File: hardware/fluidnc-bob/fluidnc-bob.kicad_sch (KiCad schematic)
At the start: 45 parts, among them J1 5V-IN, J10 LIM-Z, J11 PROBE, J2 X-DRV, J3 Y-DRV, J4 Z-DRV, J5 LIM-X, J6 LIM-Y, J7 RELAY, J8 AUX, J9 SD, Q1 2N7000, U1 SN74HC541N

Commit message: F1: generic 1-2A fast fuse on wire pads instead of polyfuse
Drew is soldering in a glass fuse (multimeter spare) by its pigtails;
the GS1A crowbar still blows it on reverse polarity. ERC clean,
netlist re-verified.

Co-Authored-By: Claude Fable 5 <noreply@anthropic.com>
Claude-Session: https://claude.ai/code/session_01VS3q9dMLBayBFkECVEvZ78
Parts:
- F1: value MF-R110 1.1A -> Fuse 1.5A fast; footprint Fuse:Fuse_Bourns_MF-RG300 -> fluidnc-bob:WirePads_1x02_P5.08mm
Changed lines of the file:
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@@
   (symbol (lib_id "bob:Fuse_H") (at 53.34 96.52 0) (unit 1) (exclude_from_sim no) (in_bom yes) (on_board yes) (dnp no)
     (property "Reference" "F1" (at 55.88 90.17 0) (effects (font (size 1.27 1.27))))
-    (property "Value" "MF-R110 1.1A" (at 55.88 102.86999999999999 0) (effects (font (size 1.27 1.27))))
-    (property "Footprint" "Fuse:Fuse_Bourns_MF-RG300" (at 53.34 96.52 0) (effects (font (size 1.27 1.27)) hide))
+    (property "Value" "Fuse 1.5A fast" (at 55.88 102.86999999999999 0) (effects (font (size 1.27 1.27))))
+    (property "Footprint" "fluidnc-bob:WirePads_1x02_P5.08mm" (at 53.34 96.52 0) (effects (font (size 1.27 1.27)) hide))
     (property "Datasheet" "" (at 53.34 96.52 0) (effects (font (size 1.27 1.27)) hide))
     (pin "1")

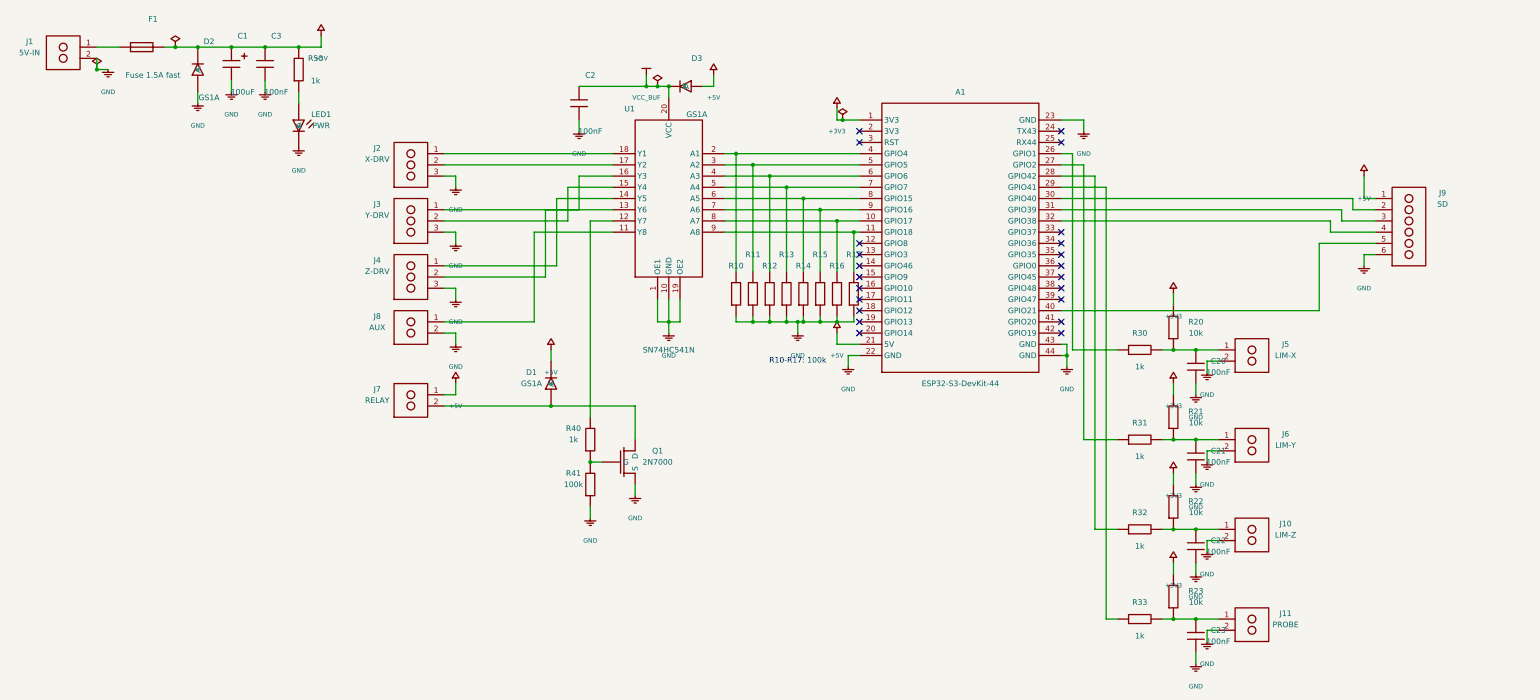
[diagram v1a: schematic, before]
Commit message: Schematic: official KiCad power symbols, labels tight to symbols
GND/+5V/+3V3/PWR_FLAG now come verbatim from KiCad's power library
(only the project-specific VCC_BUF rail stays custom). Ref/value text
placed snug beside each symbol with proper justification instead of
floating above/below. ERC clean, netlist re-verified.

Co-Authored-By: Claude Fable 5 <noreply@anthropic.com>
Claude-Session: https://claude.ai/code/session_01VS3q9dMLBayBFkECVEvZ78
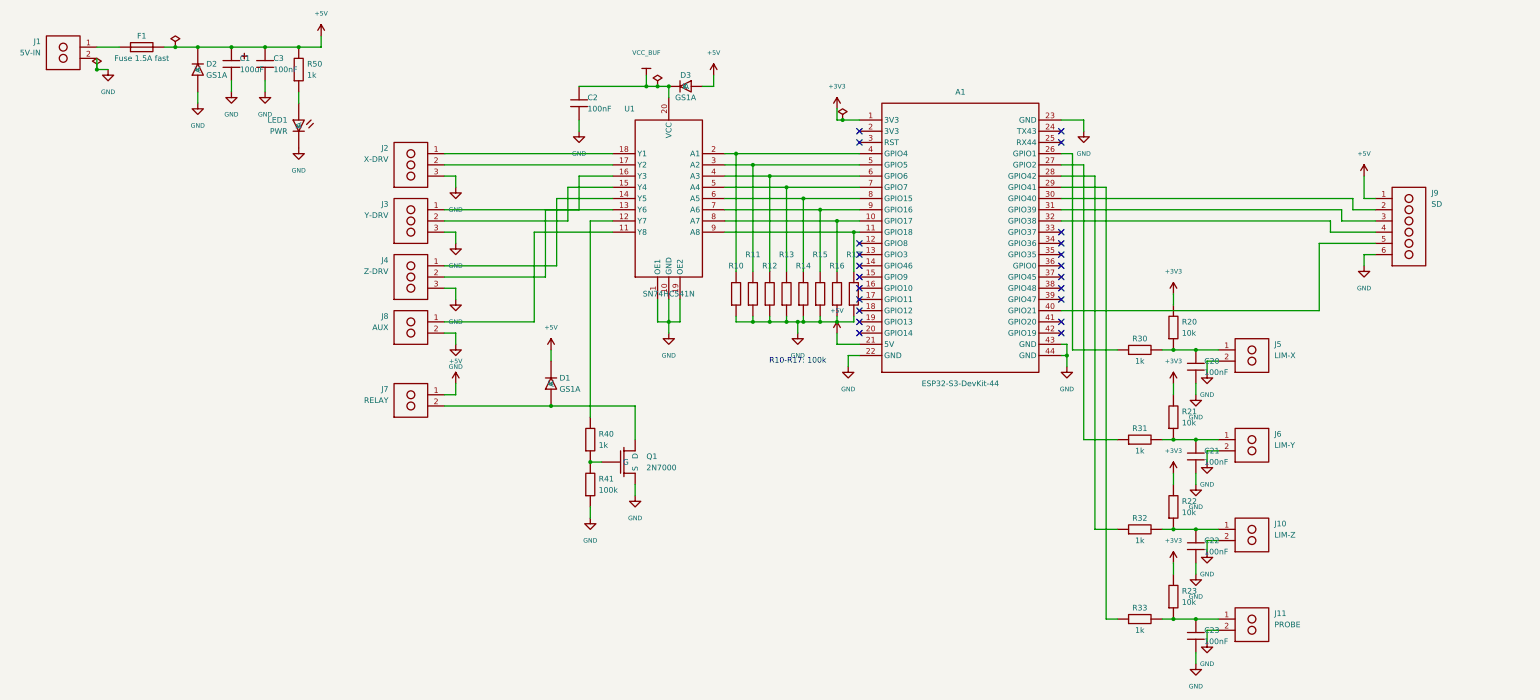
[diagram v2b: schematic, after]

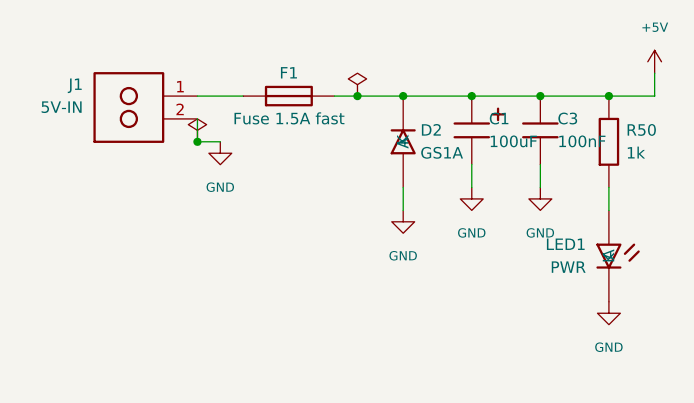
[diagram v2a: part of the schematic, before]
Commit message: F1: Littelfuse 1210L150/16WR PTC polyfuse (found in bin)
1.5A hold / ~3A trip, 16V, 1210 SMD — self-resetting, back to the
original polyfuse intent. ERC clean, netlist re-verified.

Co-Authored-By: Claude Fable 5 <noreply@anthropic.com>
Claude-Session: https://claude.ai/code/session_01VS3q9dMLBayBFkECVEvZ78
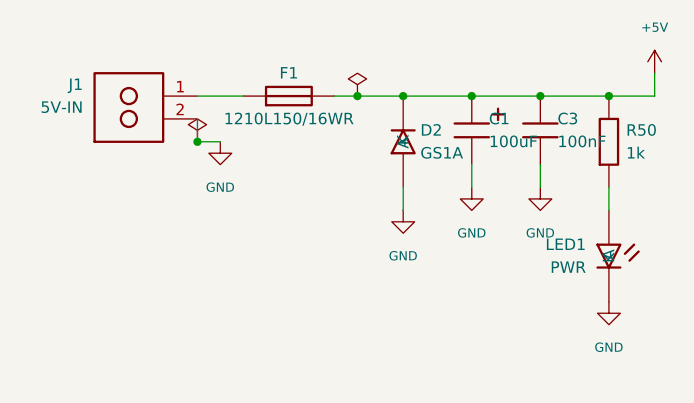
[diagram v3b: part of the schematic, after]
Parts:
- F1: value Fuse 1.5A fast -> 1210L150/16WR; footprint fluidnc-bob:WirePads_1x02_P5.08mm -> Fuse:Fuse_1210_3225Metric
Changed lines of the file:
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@@
   (symbol (lib_id "bob:Fuse_H") (at 53.34 96.52 0) (unit 1) (exclude_from_sim no) (in_bom yes) (on_board yes) (dnp no)
     (property "Reference" "F1" (at 53.34 93.97999999999999 0) (effects (font (size 1.27 1.27))))
-    (property "Value" "Fuse 1.5A fast" (at 53.34 99.06 0) (effects (font (size 1.27 1.27))))
-    (property "Footprint" "fluidnc-bob:WirePads_1x02_P5.08mm" (at 53.34 96.52 0) (effects (font (size 1.27 1.27)) hide))
+    (property "Value" "1210L150/16WR" (at 53.34 99.06 0) (effects (font (size 1.27 1.27))))
+    (property "Footprint" "Fuse:Fuse_1210_3225Metric" (at 53.34 96.52 0) (effects (font (size 1.27 1.27)) hide))
     (property "Datasheet" "" (at 53.34 96.52 0) (effects (font (size 1.27 1.27)) hide))
     (pin "1")

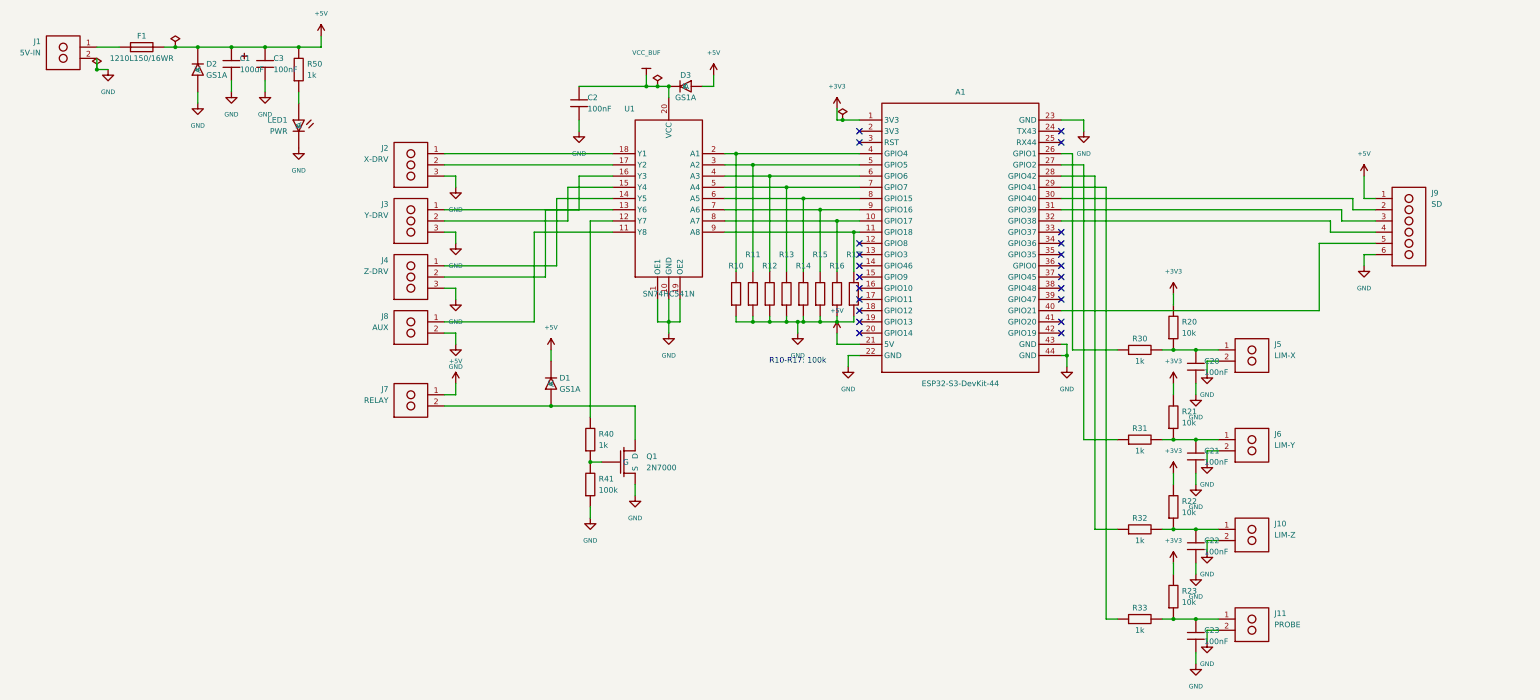
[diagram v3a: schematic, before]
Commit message: Schematic readability: crossing-free right side, labeled outputs
- J9 (SD) moved beside the devkit, straight drops from the SD pins;
  pad order now SCK/MISO/MOSI/CS/5V/GND
- Limit/probe conditioning fanned far right with non-crossing lanes
- U1 outputs use net labels on both ends (XSTEP..AUX1, SPIN5) instead
  of crossing L-wires between buffer and pad groups

ERC clean, netlist re-verified.

Co-Authored-By: Claude Fable 5 <noreply@anthropic.com>
Claude-Session: https://claude.ai/code/session_01VS3q9dMLBayBFkECVEvZ78
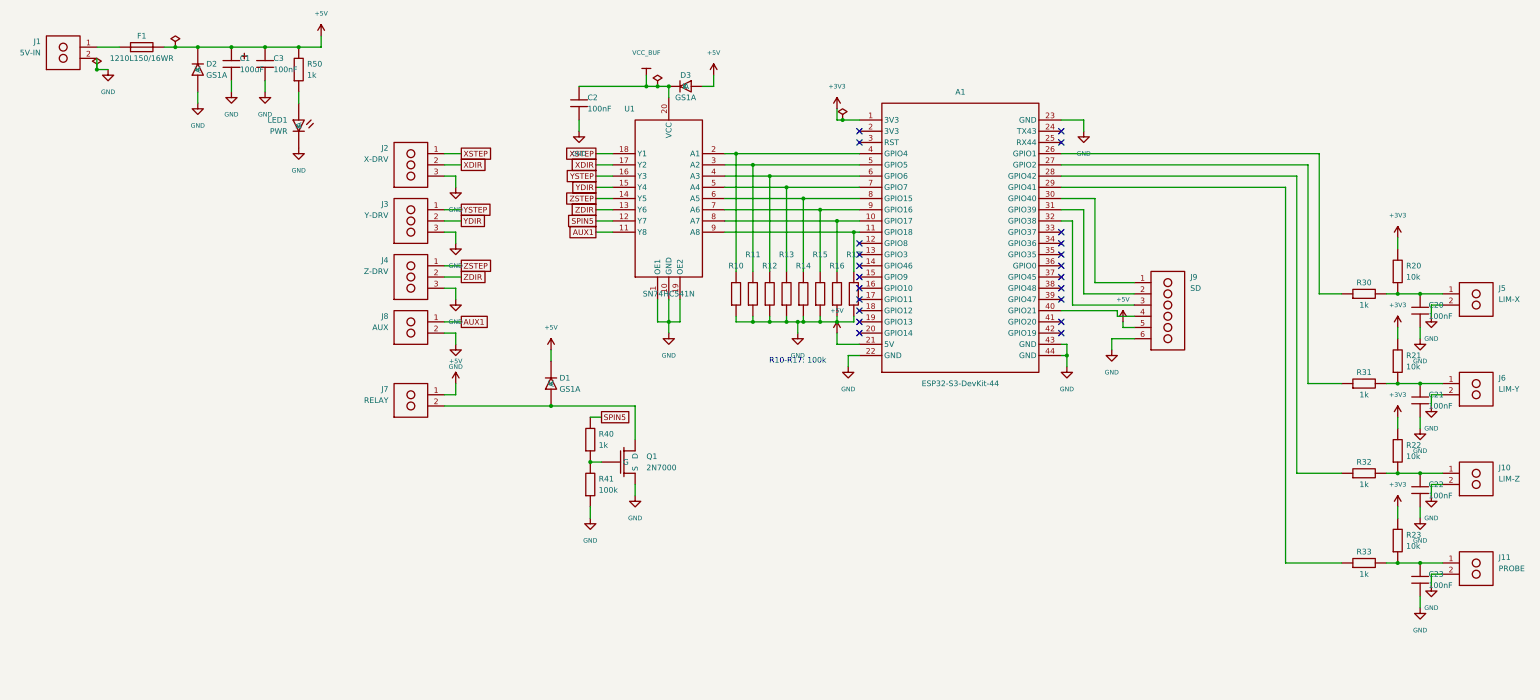
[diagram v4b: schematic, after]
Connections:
- net +5V: now also J9.5; no longer J9.1
- net at A1.30 (GPIO40): now also J9.1; no longer J9.2
- net at A1.31 (GPIO39): now also J9.2; no longer J9.3
- net at A1.32 (GPIO38): now also J9.3; no longer J9.4
- net at A1.40 (GPIO21): now also J9.4; no longer J9.5
- net SPIN5: now reaches R40.1, U1.12 (Y7)
- net AUX1: now reaches J8.1, U1.11 (Y8)
- net YSTEP: now reaches J3.1, U1.16 (Y3)
- net YSTEP: no longer J4.2, U1.13 (Y6)
- net ZSTEP: now reaches J4.1, U1.14 (Y5)
- net YDIR: now reaches J3.2, U1.15 (Y4)
- net XDIR: now reaches J2.2, U1.17 (Y2)
- net XSTEP: now reaches J2.1, U1.18 (Y1)
- new net ZDIR: J4.2, U1.13 (Y6)

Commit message: Q1: 2N2222A NPN replaces 2N7000 (bin part)
Proper NPN symbol (E/B/C), NGATE net renamed NBASE. R40 1k base
resistor gives ~3.5mA drive = forced beta 20 at the 70mA coil —
hard saturation, no resistor changes needed. R41 stays as B-E
pulldown. BOM notes the E-B-C vs C-B-E TO-92 variant trap.

Co-Authored-By: Claude Fable 5 <noreply@anthropic.com>
Claude-Session: https://claude.ai/code/session_01VS3q9dMLBayBFkECVEvZ78
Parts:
- removed Q1: 2N7000, Package_TO_SOT_THT:TO-92_Inline, symbol bob:Q_NMOS
- added Q1: 2N2222A, Package_TO_SOT_THT:TO-92_Inline, symbol bob:Q_NPN
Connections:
- net GND: now also Q1.1 (E)
- net at R40.2, R41.1: now also Q1.2 (B)
- net at D1.2 (A), J7.2: now also Q1.3 (C)
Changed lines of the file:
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@@
     (instances (project "fluidnc-bob" (path "/90005a82-a137-521e-8a64-2e75a611a04d" (reference "J9") (unit 1))))
   )
-  (symbol (lib_id "bob:Q_NMOS") (at 162.56 190.5 0) (unit 1) (exclude_from_sim no) (in_bom yes) (on_board yes) (dnp no)
+  (symbol (lib_id "bob:Q_NPN") (at 162.56 190.5 0) (unit 1) (exclude_from_sim no) (in_bom yes) (on_board yes) (dnp no)
     (property "Reference" "Q1" (at 167.64000000000001 189.23 0) (effects (font (size 1.27 1.27)) (justify left)))
-    (property "Value" "2N7000" (at 167.64000000000001 191.77 0) (effects (font (size 1.27 1.27)) (justify left)))
+    (property "Value" "2N2222A" (at 167.64000000000001 191.77 0) (effects (font (size 1.27 1.27)) (justify left)))
     (property "Footprint" "Package_TO_SOT_THT:TO-92_Inline" (at 162.56 190.5 0) (effects (font (size 1.27 1.27)) hide))
     (property "Datasheet" "" (at 162.56 190.5 0) (effects (font (size 1.27 1.27)) hide))

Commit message: Q1: MMBT2222A SOT-23 (SMD, minimizes drilling for homemade board)
SOT-23 pin numbering (1=B 2=E 3=C) applied to symbol and netlist —
different from the TO-92 E-B-C order. ERC clean, netlist re-verified.

Co-Authored-By: Claude Fable 5 <noreply@anthropic.com>
Claude-Session: https://claude.ai/code/session_01VS3q9dMLBayBFkECVEvZ78
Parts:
- Q1: value 2N2222A -> MMBT2222A; footprint Package_TO_SOT_THT:TO-92_Inline -> Package_TO_SOT_SMD:SOT-23
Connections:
- net GND: now also Q1.2 (E); no longer Q1.1 (E)
- net at R40.2, R41.1: now also Q1.1 (B); no longer Q1.2 (B)
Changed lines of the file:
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@@
   (symbol (lib_id "bob:Q_NPN") (at 162.56 190.5 0) (unit 1) (exclude_from_sim no) (in_bom yes) (on_board yes) (dnp no)
     (property "Reference" "Q1" (at 167.64000000000001 189.23 0) (effects (font (size 1.27 1.27)) (justify left)))
-    (property "Value" "2N2222A" (at 167.64000000000001 191.77 0) (effects (font (size 1.27 1.27)) (justify left)))
-    (property "Footprint" "Package_TO_SOT_THT:TO-92_Inline" (at 162.56 190.5 0) (effects (font (size 1.27 1.27)) hide))
+    (property "Value" "MMBT2222A" (at 167.64000000000001 191.77 0) (effects (font (size 1.27 1.27)) (justify left)))
+    (property "Footprint" "Package_TO_SOT_SMD:SOT-23" (at 162.56 190.5 0) (effects (font (size 1.27 1.27)) hide))
     (property "Datasheet" "" (at 162.56 190.5 0) (effects (font (size 1.27 1.27)) hide))
+    (pin "2")
     (pin "1")
-    (pin "2")
     (pin "3")
     (instances (project "fluidnc-bob" (path "/90005a82-a137-521e-8a64-2e75a611a04d" (reference "Q1") (unit 1))))
